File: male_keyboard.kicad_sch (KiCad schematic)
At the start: 1 part, among them J1 Elite-Pi Microcontroller

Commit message: 1504202502
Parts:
- added J2: AudioJack4, Keebio-Parts:TRRS-PJ-320A, symbol Connector_Audio:AudioJack4
- added SW1: SW_MEC_5G, Button_Switch_Keyboard:SW_Cherry_MX_1.00u_PCB, symbol Switch:SW_MEC_5G
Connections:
- net GND: now also J1.23 (Pin_23), J2.1, J2.2, SW1.2; no longer J1.2 (Pin_2)
- net at J1.19 (Pin_19): now also SW1.1
- net at J1.21 (Pin_21): now also J2.4
- new net: J1.2 (Pin_2), J2.3
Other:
- moved on the sheet: J1

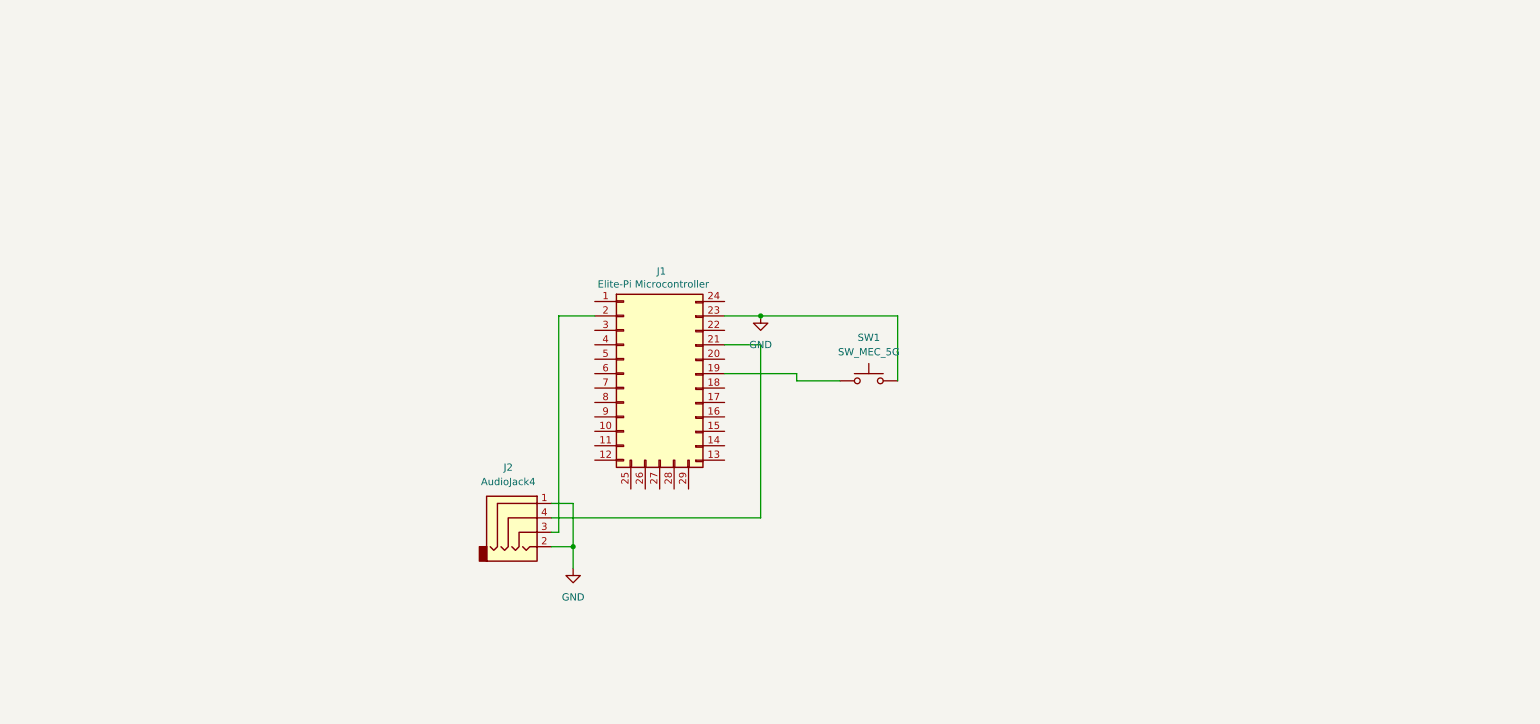
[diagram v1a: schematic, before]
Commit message: Copy DASBOB matrix
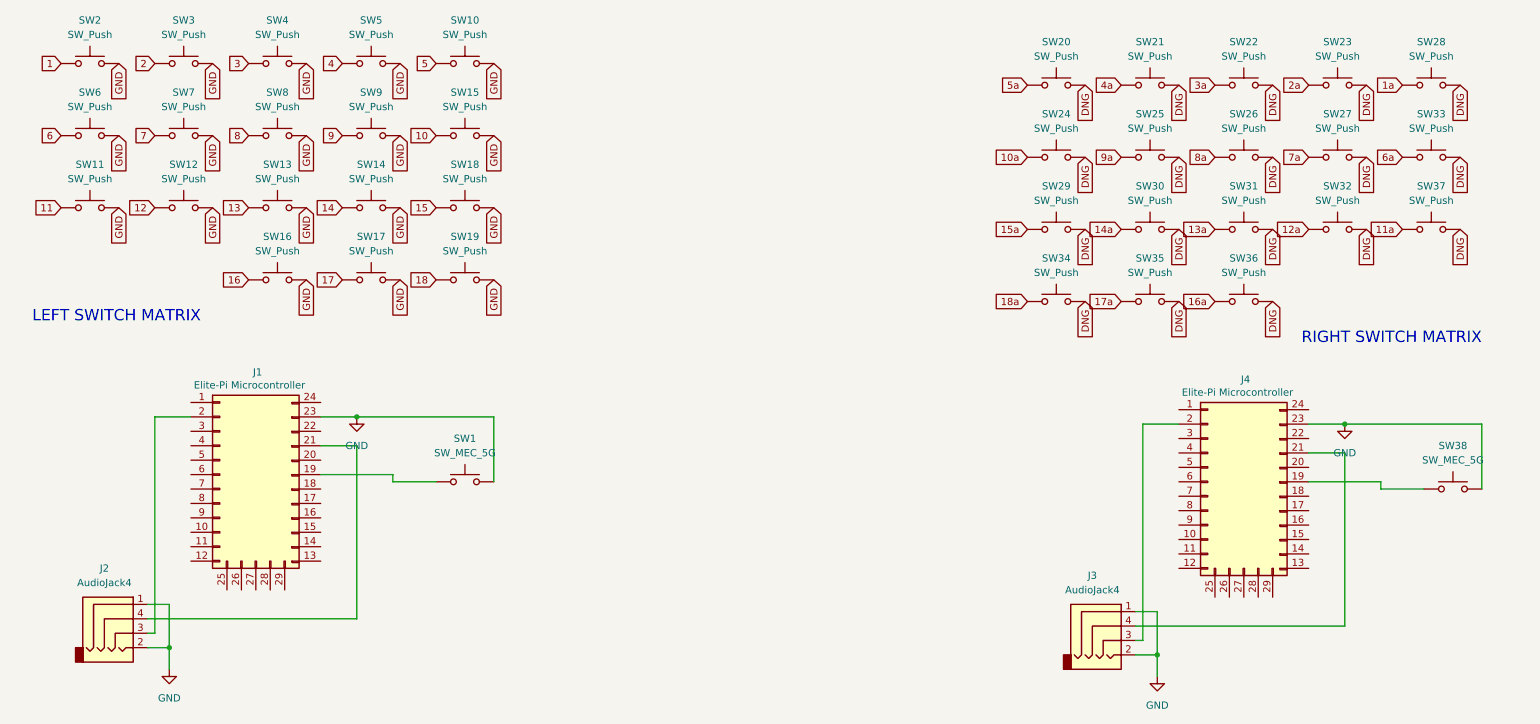
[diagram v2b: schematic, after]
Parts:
- added J3: AudioJack4, Keebio-Parts:TRRS-PJ-320A, symbol Connector_Audio:AudioJack4
- added J4: Elite-Pi Microcontroller, Keebio-Parts:Elite-C, symbol Connector_Generic:Conn_01x12
- added SW10, SW11, SW12, SW13, SW14, SW15, SW16, SW17, SW18, SW19, SW20, SW21, SW22, SW23, SW24, SW25, SW26, SW27, SW28, SW29, SW3, SW30, SW31, SW32, SW33, SW34, SW35, SW36, SW37, SW4, SW5, SW6, SW7, SW8, SW9: SW_Push, Beibob:Kailh_socket_PG1350_optional, symbol Switch:SW_Push
- added SW2: SW_Push, Button_Switch_Keyboard:SW_Cherry_MX_1.00u_PCB, symbol Switch:SW_Push
- added SW38: SW_MEC_5G, Button_Switch_Keyboard:SW_Cherry_MX_1.00u_PCB, symbol Switch:SW_MEC_5G
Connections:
- net GND: now also J3.1, J3.2, J4.23 (Pin_23), SW10.2, SW11.2, SW12.2, SW13.2, SW14.2, SW15.2, SW16.2, SW17.2, SW18.2, SW19.2, SW2.2, SW3.2, SW38.2, SW4.2, SW5.2, SW6.2, SW7.2, SW8.2, SW9.2
- new net: J4.19 (Pin_19), SW38.1
- new net: J3.3, J4.2 (Pin_2)
- new net: J3.4, J4.21 (Pin_21)
- new net 1: SW2.1
- new net 10: SW15.1
- new net 10a: SW24.1
- new net 11: SW11.1
- new net 11a: SW37.1
- new net 12: SW12.1
- new net 12a: SW32.1
- new net 13: SW13.1
- new net 13a: SW31.1
- new net 14: SW14.1
- new net 14a: SW30.1
- new net 15: SW18.1
- new net 15a: SW29.1
- new net 16: SW16.1
- new net 16a: SW36.1
- new net 17: SW17.1
- new net 17a: SW35.1
- new net 18: SW19.1
- new net 18a: SW34.1
- new net 1a: SW28.1
- new net 2: SW3.1
- new net 2a: SW23.1
- new net 3: SW4.1
- new net 3a: SW22.1
- new net 4: SW5.1
- new net 4a: SW21.1
- new net 5: SW10.1
- new net 5a: SW20.1
- new net 6: SW6.1
- new net 6a: SW33.1
- new net 7: SW7.1
- new net 7a: SW27.1
- new net 8: SW8.1
- new net 8a: SW26.1
- new net 9: SW9.1
- new net 9a: SW25.1
- new net DNG: SW20.2, SW21.2, SW22.2, SW23.2, SW24.2, SW25.2, SW26.2, SW27.2, SW28.2, SW29.2, SW30.2, SW31.2, SW32.2, SW33.2, SW34.2, SW35.2, SW36.2, SW37.2
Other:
- note added: "LEFT SWITCH MATRIX"
- note added: "RIGHT SWITCH MATRIX"
- moved on the sheet: J1, J2, SW1

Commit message: left side footprints
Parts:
- SW10, SW11, SW12, SW13, SW14, SW15, SW16, SW17, SW18, SW19, SW3, SW4, SW5, SW6, SW7, SW8, SW9: footprint Beibob:Kailh_socket_PG1350_optional -> Button_Switch_Keyboard:SW_Cherry_MX_1.00u_PCB
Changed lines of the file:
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@@
 			)
 		)
-		(property "Footprint" "Beibob:Kailh_socket_PG1350_optional"
+		(property "Footprint" "Button_Switch_Keyboard:SW_Cherry_MX_1.00u_PCB"
 			(at 62.23 46.99 0)
 			(effects
@@
 			)
 		)
-		(property "Footprint" "Beibob:Kailh_socket_PG1350_optional"
+		(property "Footprint" "Button_Switch_Keyboard:SW_Cherry_MX_1.00u_PCB"
 			(at 78.74 21.59 0)
 			(effects
@@
 			)
 		)
-		(property "Footprint" "Beibob:Kailh_socket_PG1350_optional"
+		(property "Footprint" "Button_Switch_Keyboard:SW_Cherry_MX_1.00u_PCB"
 			(at 78.74 46.99 0)
 			(effects
@@
 			)
 		)
-		(property "Footprint" "Beibob:Kailh_socket_PG1350_optional"
+		(property "Footprint" "Button_Switch_Keyboard:SW_Cherry_MX_1.00u_PCB"
 			(at 62.23 21.59 0)
 			(effects
@@
 			)
 		)
-		(property "Footprint" "Beibob:Kailh_socket_PG1350_optional"
+		(property "Footprint" "Button_Switch_Keyboard:SW_Cherry_MX_1.00u_PCB"
 			(at 78.74 34.29 0)
 			(effects
@@
 			)
 		)
-		(property "Footprint" "Beibob:Kailh_socket_PG1350_optional"
+		(property "Footprint" "Button_Switch_Keyboard:SW_Cherry_MX_1.00u_PCB"
 			(at 95.25 59.69 0)
 			(effects
@@
 			)
 		)
-		(property "Footprint" "Beibob:Kailh_socket_PG1350_optional"
+		(property "Footprint" "Button_Switch_Keyboard:SW_Cherry_MX_1.00u_PCB"
 			(at 29.21 34.29 0)
 			(effects
@@
 			)
 		)
-		(property "Footprint" "Beibob:Kailh_socket_PG1350_optional"
+		(property "Footprint" "Button_Switch_Keyboard:SW_Cherry_MX_1.00u_PCB"
 			(at 95.25 46.99 0)
 			(effects
@@
 			)
 		)
-		(property "Footprint" "Beibob:Kailh_socket_PG1350_optional"
+		(property "Footprint" "Button_Switch_Keyboard:SW_Cherry_MX_1.00u_PCB"
 			(at 45.72 46.99 0)
 			(effects
@@
 			)
 		)
-		(property "Footprint" "Beibob:Kailh_socket_PG1350_optional"
+		(property "Footprint" "Button_Switch_Keyboard:SW_Cherry_MX_1.00u_PCB"
 			(at 29.21 46.99 0)
 			(effects
@@
 			)
 		)
-		(property "Footprint" "Beibob:Kailh_socket_PG1350_optional"
+		(property "Footprint" "Button_Switch_Keyboard:SW_Cherry_MX_1.00u_PCB"
 			(at 95.25 21.59 0)
 			(effects
@@
 			)
 		)
-		(property "Footprint" "Beibob:Kailh_socket_PG1350_optional"
+		(property "Footprint" "Button_Switch_Keyboard:SW_Cherry_MX_1.00u_PCB"
 			(at 78.74 59.69 0)
 			(effects
@@
 			)
 		)
-		(property "Footprint" "Beibob:Kailh_socket_PG1350_optional"
+		(property "Footprint" "Button_Switch_Keyboard:SW_Cherry_MX_1.00u_PCB"
 			(at 62.23 34.29 0)
 			(effects
@@
 			)
 		)
-		(property "Footprint" "Beibob:Kailh_socket_PG1350_optional"
+		(property "Footprint" "Button_Switch_Keyboard:SW_Cherry_MX_1.00u_PCB"
 			(at 62.23 59.69 0)
 			(effects
@@
 			)
 		)
-		(property "Footprint" "Beibob:Kailh_socket_PG1350_optional"
+		(property "Footprint" "Button_Switch_Keyboard:SW_Cherry_MX_1.00u_PCB"
 			(at 45.72 34.29 0)
 			(effects
@@
 			)
 		)
-		(property "Footprint" "Beibob:Kailh_socket_PG1350_optional"
+		(property "Footprint" "Button_Switch_Keyboard:SW_Cherry_MX_1.00u_PCB"
 			(at 95.25 34.29 0)
 			(effects
@@
 			)
 		)
-		(property "Footprint" "Beibob:Kailh_socket_PG1350_optional"
+		(property "Footprint" "Button_Switch_Keyboard:SW_Cherry_MX_1.00u_PCB"
 			(at 45.72 21.59 0)
 			(effects
